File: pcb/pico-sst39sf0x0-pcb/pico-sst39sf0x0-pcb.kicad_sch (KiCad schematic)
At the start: 52 parts, among them Q1 BSS138, Q10 BSS138, Q11 BSS138, Q12 BSS138, Q13 BSS138, Q14 BSS138, Q15 BSS138, Q16 BSS138, Q17 BSS138, Q18 BSS138, Q19 BSS138, Q2 BSS138, Q20 BSS138, Q21 BSS138, Q22 BSS138, Q23 BSS138, Q24 BSS138, Q3 BSS138, Q4 BSS138, Q5 BSS138, Q6 BSS138, Q7 BSS138, Q8 BSS138, Q9 BSS138, SW1 SW_Push, U1 74HC573, U2 SST39SF040, U3 74HC573, U4 Pico, U5 74HC573

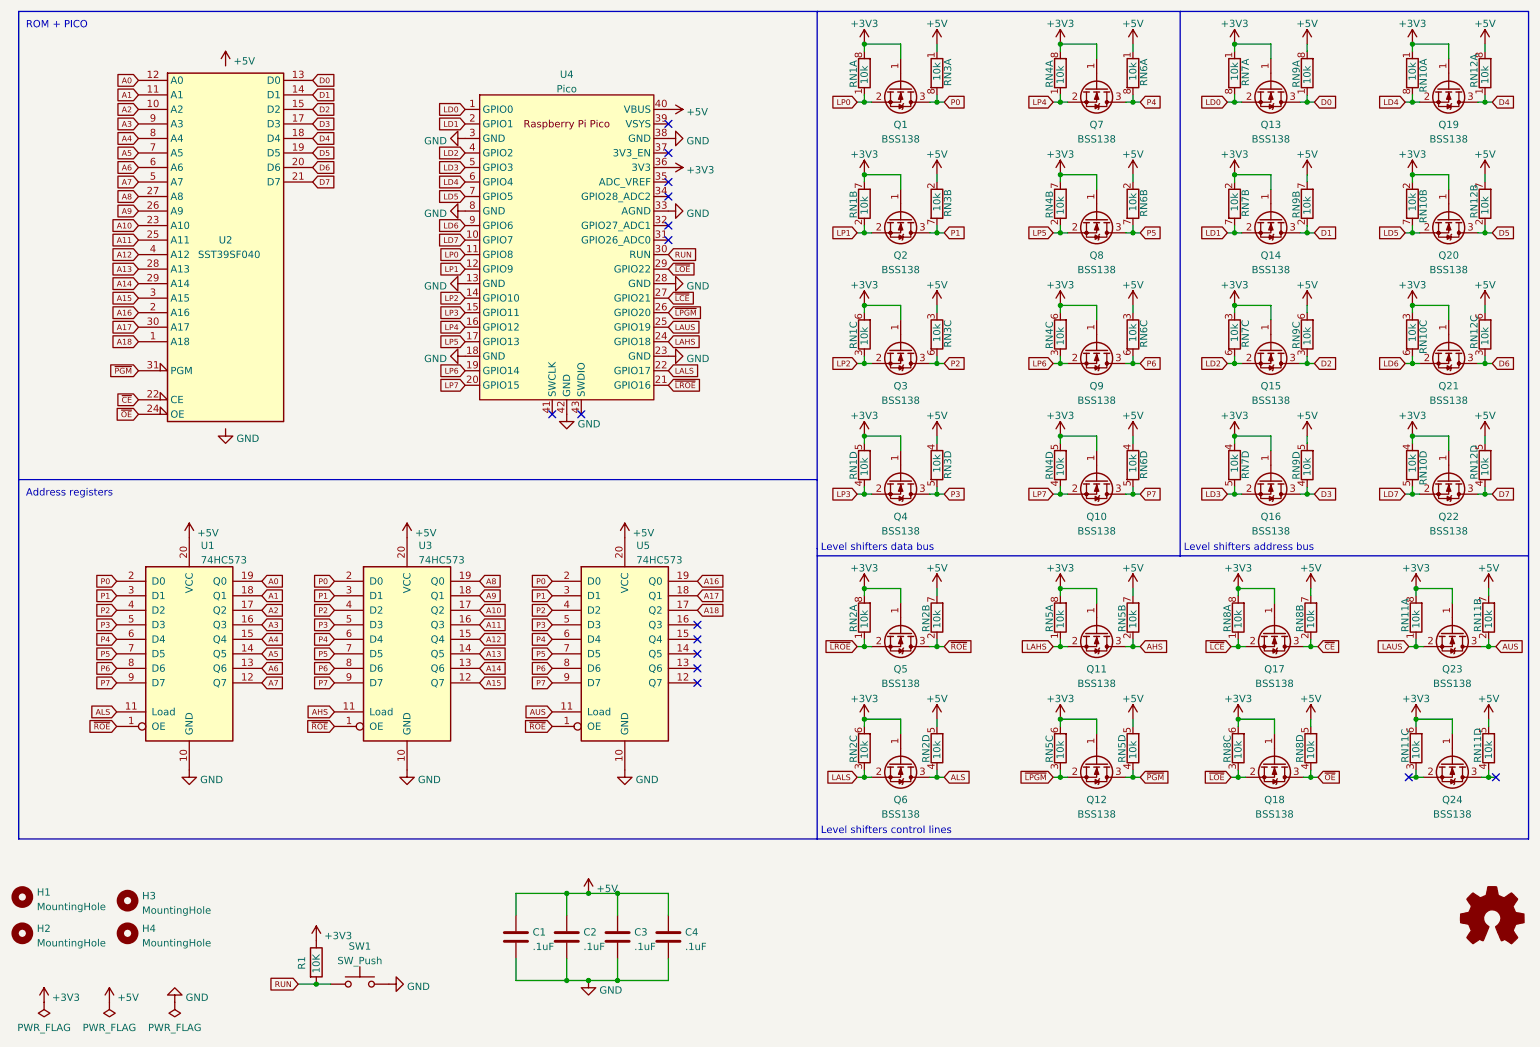
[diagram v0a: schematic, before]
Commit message: Adding LEDs and putting 10k resistor on backside
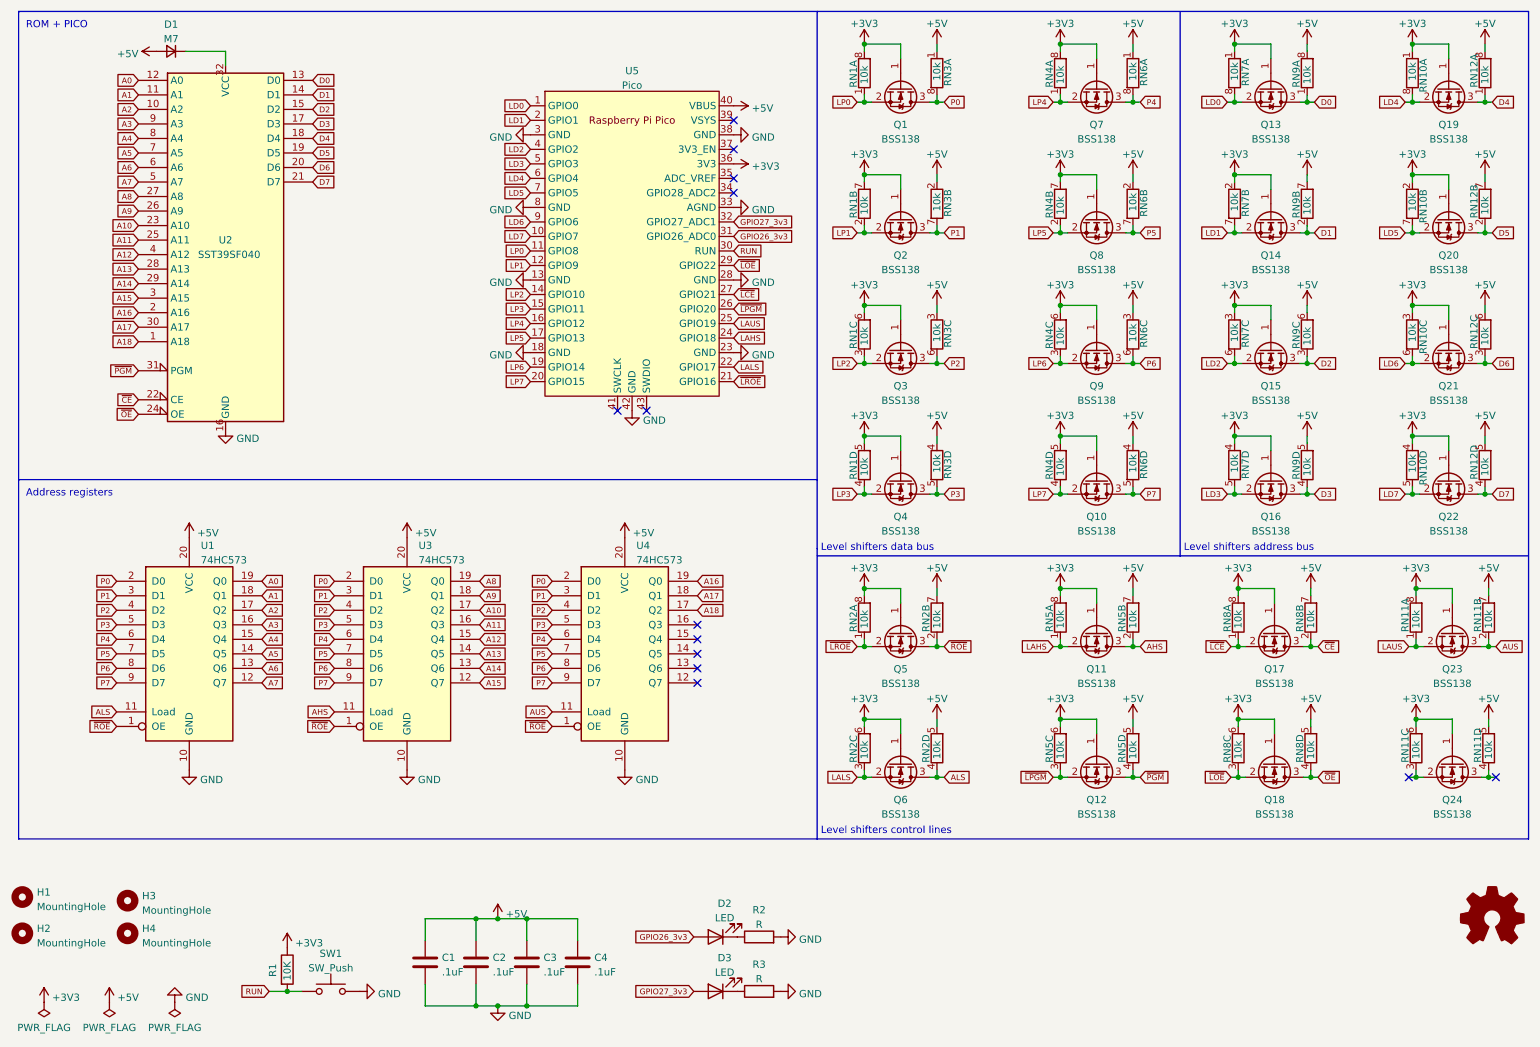
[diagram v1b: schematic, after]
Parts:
- added D1: M7, Diode_SMD:D_SMA, symbol Device:D_Small
- added D2, D3: LED, LED_THT:LED_D5.0mm, symbol Device:LED
- added R2, R3: R, Resistor_THT:R_Axial_DIN0207_L6.3mm_D2.5mm_P7.62mm_Horizontal, symbol Device:R
- R1: LCSC (none) -> C17414
- U2: symbol Memory_Flash:SST39SF040 -> sst39sf040:SST39SF040
- renumbered U5 to U4, U4 to U5
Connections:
- net +5V: now also D1.2 (A); no longer U2.32 (VCC)
- net GND: now also R2.2, R3.2
- net GPIO26_3v3: now reaches U5.31 (GPIO26_ADC0)
- net GPIO26_3v3: now also D2.2 (A)
- net GPIO27_3v3: now reaches U5.32 (GPIO27_ADC1)
- net GPIO27_3v3: now also D3.2 (A)
- new net: D1.1 (K), U2.32 (VCC)
- new net: D3.1 (K), R3.1
- new net: D2.1 (K), R2.1
- no-connect marks 15 -> 13
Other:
- moved on the sheet: C1, C2, C3, C4, R1, SW1, U5

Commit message: Revision 2 of the PCB (#11)
* Initial commit revision 2

* Revising top case

* Updating photo

* Updating photos PCBs
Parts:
- C1, C2, C3, C4: LCSC Part # (none) -> C1790
- D1: LCSC Part # (none) -> C95872
- Q1, Q10, Q11, Q12, Q13, Q14, Q15, Q16, Q17, Q18, Q19, Q2, Q20, Q21, Q22, Q23, Q24, Q3, Q4, Q5, Q6, Q7, Q8, Q9: LCSC Part # (none) -> C78284
- R1: LCSC Part # (none) -> C17414
- R2, R3: value R -> 560; footprint Resistor_THT:R_Axial_DIN0207_L6.3mm_D2.5mm_P7.62mm_Horizontal -> Resistor_SMD:R_0805_2012Metric_Pad1.20x1.40mm_HandSolder; LCSC (none) -> C28636; LCSC Part # (none) -> C28636
- RN1, RN10, RN11, RN12, RN2, RN3, RN4, RN5, RN6, RN7, RN8, RN9: LCSC Part # (none) -> C110924
- U1, U3, U4: LCSC Part # (none) -> C5608
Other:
- title: (none) -> PICO SST39SF0x0 Programmer

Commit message: Tweaking lay-out PCB
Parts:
- D2: value LED -> READ
- D3: value LED -> WRITE
- U2: value SST39SF040 -> ZIF SOCKET
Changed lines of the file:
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@@
       (effects (font (size 1.27 1.27)))
     )
-    (property "Value" "SST39SF040" (at 55.88 58.42 0)
+    (property "Value" "ZIF SOCKET" (at 55.88 58.42 0)
       (effects (font (size 1.27 1.27)))
     )
@@
   (symbol (lib_id "Device:LED") (at 140.97 177.8 180) (unit 1)
     (in_bom yes) (on_board yes) (dnp no) (fields_autoplaced)
-    (property "Reference" "D2" (at 142.5575 171.9412 0)
-      (effects (font (size 1.27 1.27)))
-    )
-    (property "Value" "LED" (at 142.5575 174.4781 0)
+    (property "Reference" "D2" (at 142.5575 170.18 0)
+      (effects (font (size 1.27 1.27)))
+    )
+    (property "Value" "READ" (at 142.5575 172.72 0)
       (effects (font (size 1.27 1.27)))
     )
@@
   (symbol (lib_id "Device:LED") (at 140.97 187.325 180) (unit 1)
     (in_bom yes) (on_board yes) (dnp no) (fields_autoplaced)
-    (property "Reference" "D3" (at 142.5575 181.4662 0)
-      (effects (font (size 1.27 1.27)))
-    )
-    (property "Value" "LED" (at 142.5575 184.0031 0)
-      (effects (font (size 1.27 1.27)))
-    )
+    (property "Reference" "D3" (at 142.5575 180.34 0)
+      (effects (font (size 1.27 1.27)))
+    )
+    (property "Value" "WRITE" (at 142.5575 182.88 0)
+      (effects (font (size 1.27 1.27)))
+    )
